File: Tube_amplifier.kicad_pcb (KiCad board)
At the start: 2 copper layers, 5 x 5 mm, 2 parts, among them U1 6N2P, U2 6P14P

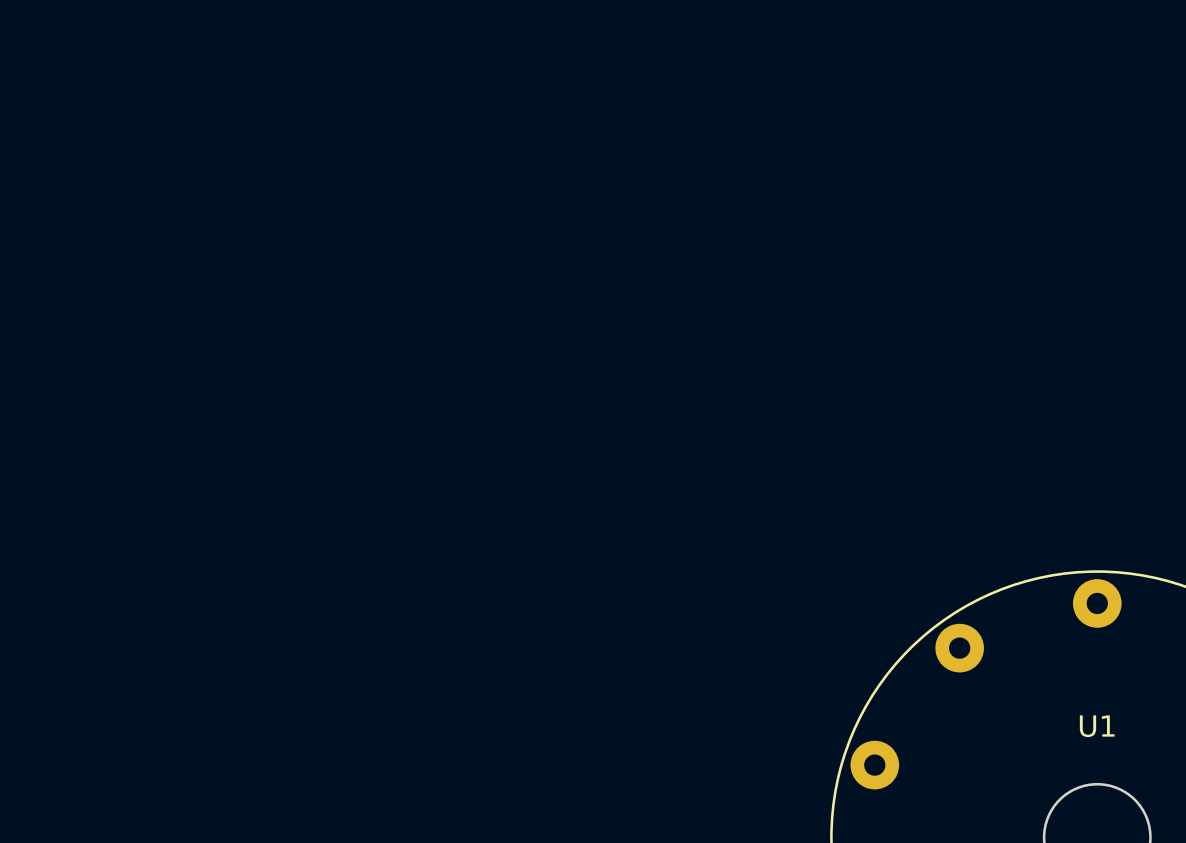
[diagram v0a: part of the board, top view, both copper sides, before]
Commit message: 7-pin socket 3d model added
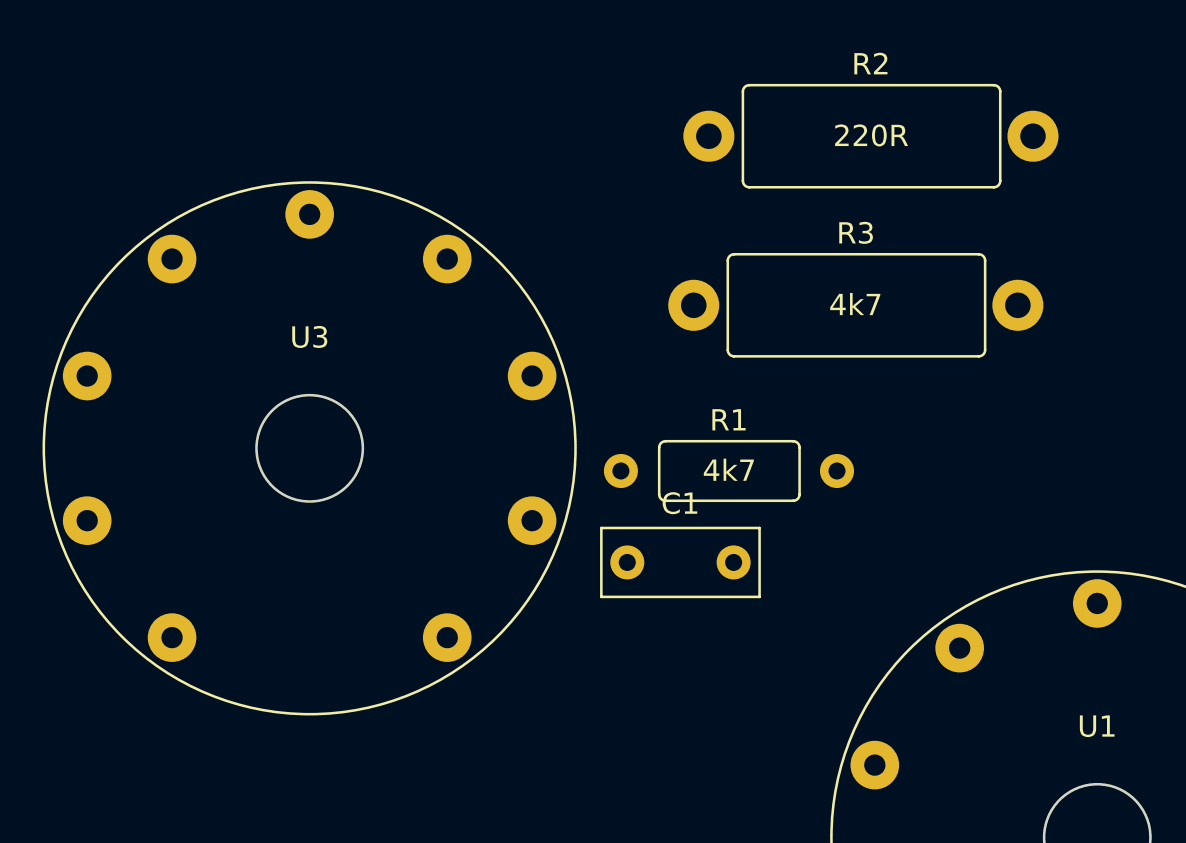
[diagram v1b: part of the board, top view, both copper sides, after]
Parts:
- added C1: 1500pF, Capacitor_THT:C_Rect_L7.2mm_W3.0mm_P5.00mm_FKS2_FKP2_MKS2_MKP2, F.Cu at (73.3, 48.1)
- added R1: 4k7, spdf1626_lib:R_THT_025W, F.Cu at (73.0, 43.8)
- added R2: 220R, spdf1626_lib:R_THT_1W, F.Cu at (77.1, 28.1)
- added R3: 4k7, spdf1626_lib:R_THT_1W, F.Cu at (76.4, 36.0)
- added U3: 6H2P, spdf1626_lib:9-pin_tube_socket, F.Cu at (58.4, 42.8)
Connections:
- U2 pad 3: unconnected-(U2-Pad3) -> Net-(U2-Pad3)
- U2 pad 7: unconnected-(U2-Pad7) -> Net-(U2-Pad7)

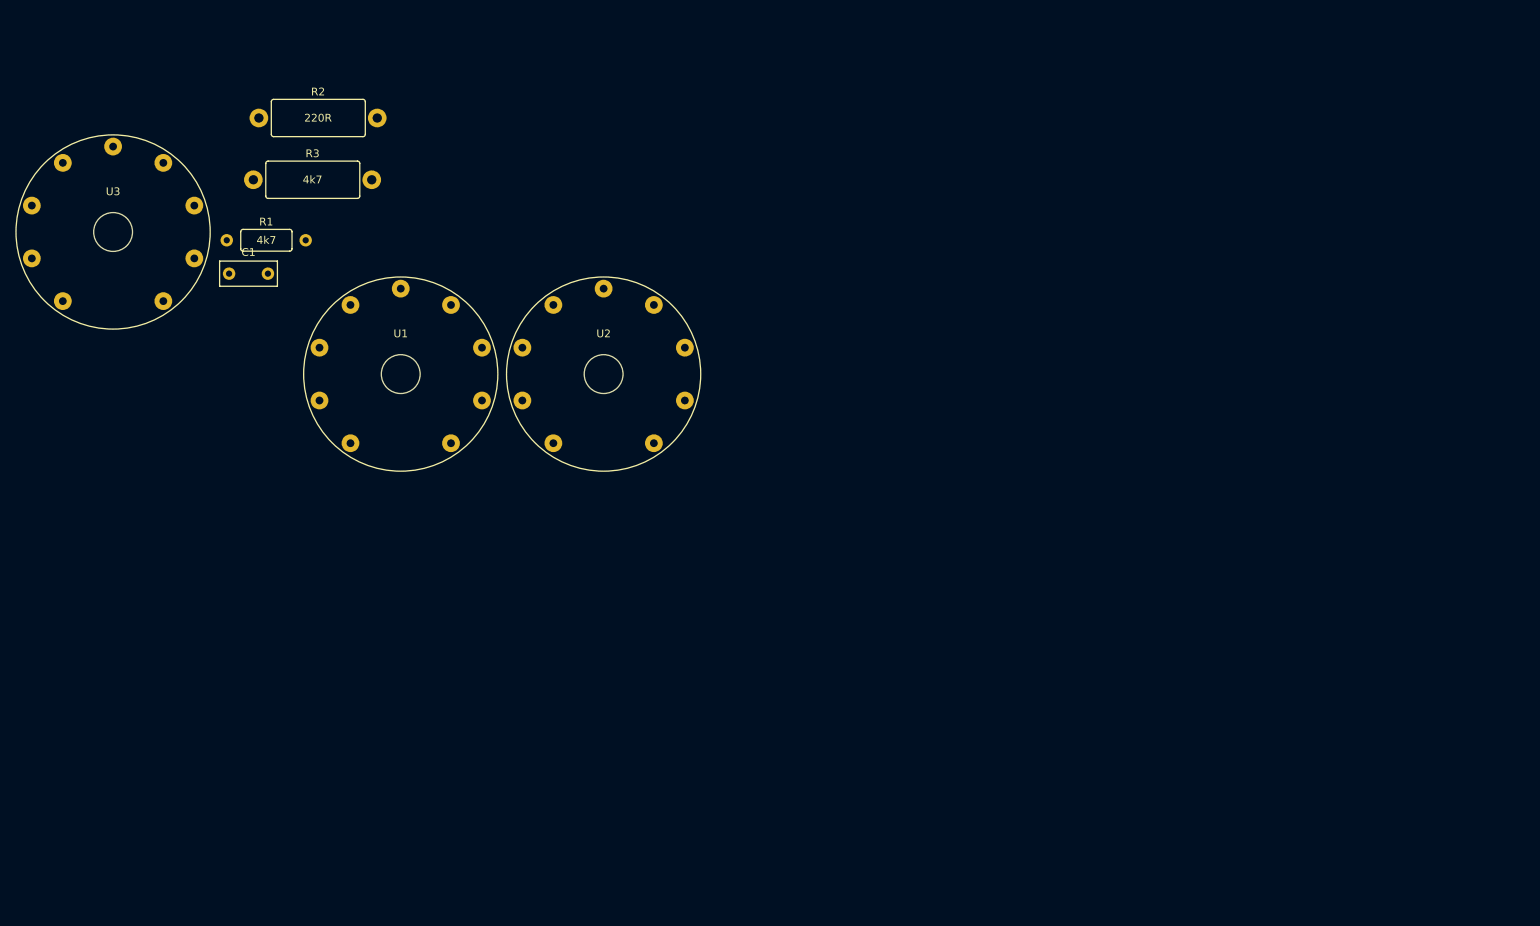
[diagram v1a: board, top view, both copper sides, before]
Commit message: Output transformer added, pcb v0.1 ready
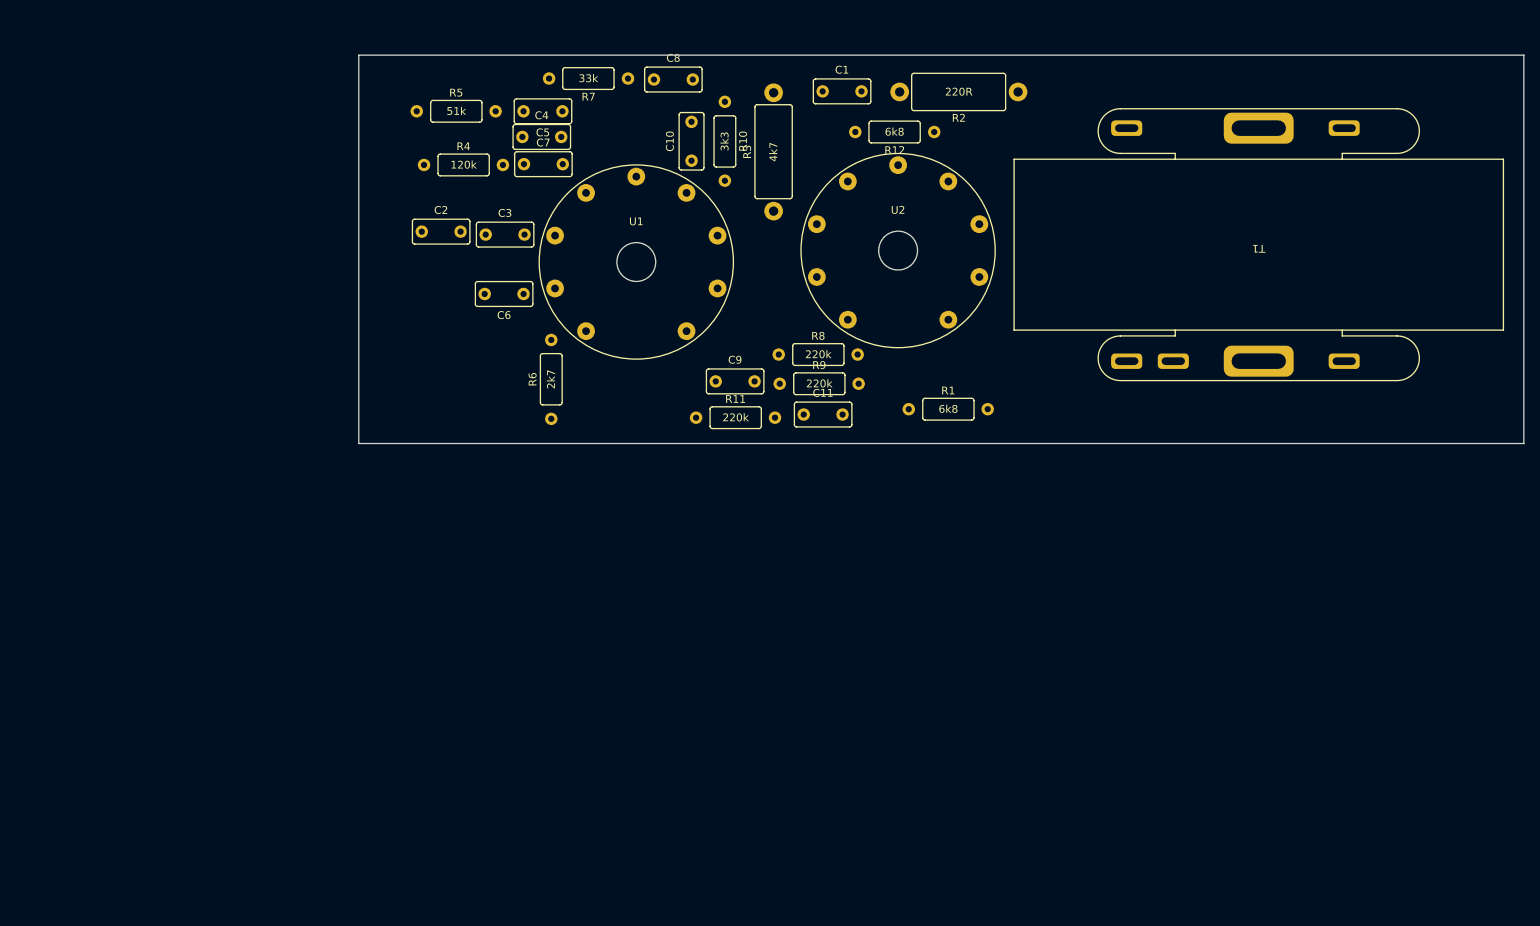
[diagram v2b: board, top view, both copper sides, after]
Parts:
- removed U3: 6H2P, spdf1626_lib:9-pin_tube_socket
- added C10: 2200pF, spdf1626_lib:C_THT_K73-17_P5.00mm, F.Cu at (132.8, 33.6)
- added C11: 3300pF, spdf1626_lib:C_THT_K73-17_P5.00mm, F.Cu at (147.3, 66.3)
- added C2: 0,047uF, spdf1626_lib:C_THT_K73-17_P5.00mm, F.Cu at (98.1, 42.7)
- added C3: 27pF, spdf1626_lib:C_THT_K73-17_P5.00mm, F.Cu at (106.3, 43.1)
- added C4: 2200pF, spdf1626_lib:C_THT_K73-17_P5.00mm, F.Cu at (111.1, 30.5)
- added C5: 4700pF, spdf1626_lib:C_THT_K73-17_P5.00mm, F.Cu at (116.2, 27.2)
- added C6: 0,01uF, spdf1626_lib:C_THT_K73-17_P5.00mm, F.Cu at (111.2, 50.7)
- added C7: 0,033uF, spdf1626_lib:C_THT_K73-17_P5.00mm, F.Cu at (111.3, 34.0)
- added C8: 2200pF, spdf1626_lib:C_THT_K73-17_P5.00mm, F.Cu at (128.0, 23.1)
- added C9: 5,6pF, spdf1626_lib:C_THT_K73-17_P5.00mm, F.Cu at (136.0, 62.0)
- added R10: 3k3, spdf1626_lib:R_THT_025W, F.Cu at (137.1, 26.0)
- added R11: 220k, spdf1626_lib:R_THT_025W, F.Cu at (133.4, 66.7)
- added R12: 6k8, spdf1626_lib:R_THT_025W, F.Cu at (164.1, 29.9)
- added R4: 120k, spdf1626_lib:R_THT_025W, F.Cu at (98.4, 34.1)
- added R5: 51k, spdf1626_lib:R_THT_025W, F.Cu at (97.5, 27.2)
- added R6: 2k7, spdf1626_lib:R_THT_025W, F.Cu at (114.8, 66.8)
- added R7: 33k, spdf1626_lib:R_THT_025W, F.Cu at (124.7, 23.0)
- added R8: 220k, spdf1626_lib:R_THT_025W, F.Cu at (144.1, 58.5)
- added R9: 220k, spdf1626_lib:R_THT_025W, F.Cu at (144.2, 62.3)
- added T1: Transformer_SP_1S, spdf1626_lib:Output_transformer, F.Cu at (205.9, 44.4)
- C1: footprint Capacitor_THT:C_Rect_L7.2mm_W3.0mm_P5.00mm_FKS2_FKP2_MKS2_MKP2 -> spdf1626_lib:C_THT_K73-17_P5.00mm
- R1: value 4k7 -> 6k8
- moved R2 97.8 mm to (174.9, 24.7), turned to 180 degrees
- moved R1 90.5 mm to (160.8, 65.6)
- moved C1 79.9 mm to (149.7, 24.7)
- moved R3 67.1 mm to (143.4, 40.1), turned to 90 degrees
- moved U2 41.1 mm to (159.4, 45.2)
- moved U1 33.6 mm to (125.7, 46.6)
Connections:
- R1 pad 1: unconnected-(R1-Pad1) -> Net-(R1-Pad1)
- R1 pad 2: unconnected-(R1-Pad2) -> Net-(R1-Pad2)
- U1 pad 1: unconnected-(U1-Pad1) -> Net-(U1-Pad1)
- U1 pad 2: unconnected-(U1-Pad2) -> Net-(U1-Pad2)
- U1 pad 3: unconnected-(U1-Pad3) -> Net-(U1-Pad3)
- U1 pad 4: unconnected-(U1-Pad4) -> +6V
- U1 pad 5: unconnected-(U1-Pad5) -> GND
- U1 pad 6: unconnected-(U1-Pad6) -> Net-(U1-Pad6)
- U1 pad 7: unconnected-(U1-Pad7) -> Net-(U1-Pad7)
- U1 pad 8: unconnected-(U1-Pad8) -> Net-(U1-Pad8)
- U2 pad 2: unconnected-(U2-Pad2) -> Net-(R1-Pad2)
- U2 pad 4: unconnected-(U2-Pad4) -> +6V
- U2 pad 5: unconnected-(U2-Pad5) -> GND
- U2 pad 9: unconnected-(U2-Pad9) -> Net-(U2-Pad9)
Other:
- board size 5 x 5 mm -> 150 x 50 mm

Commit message: 7-pin tube socket added
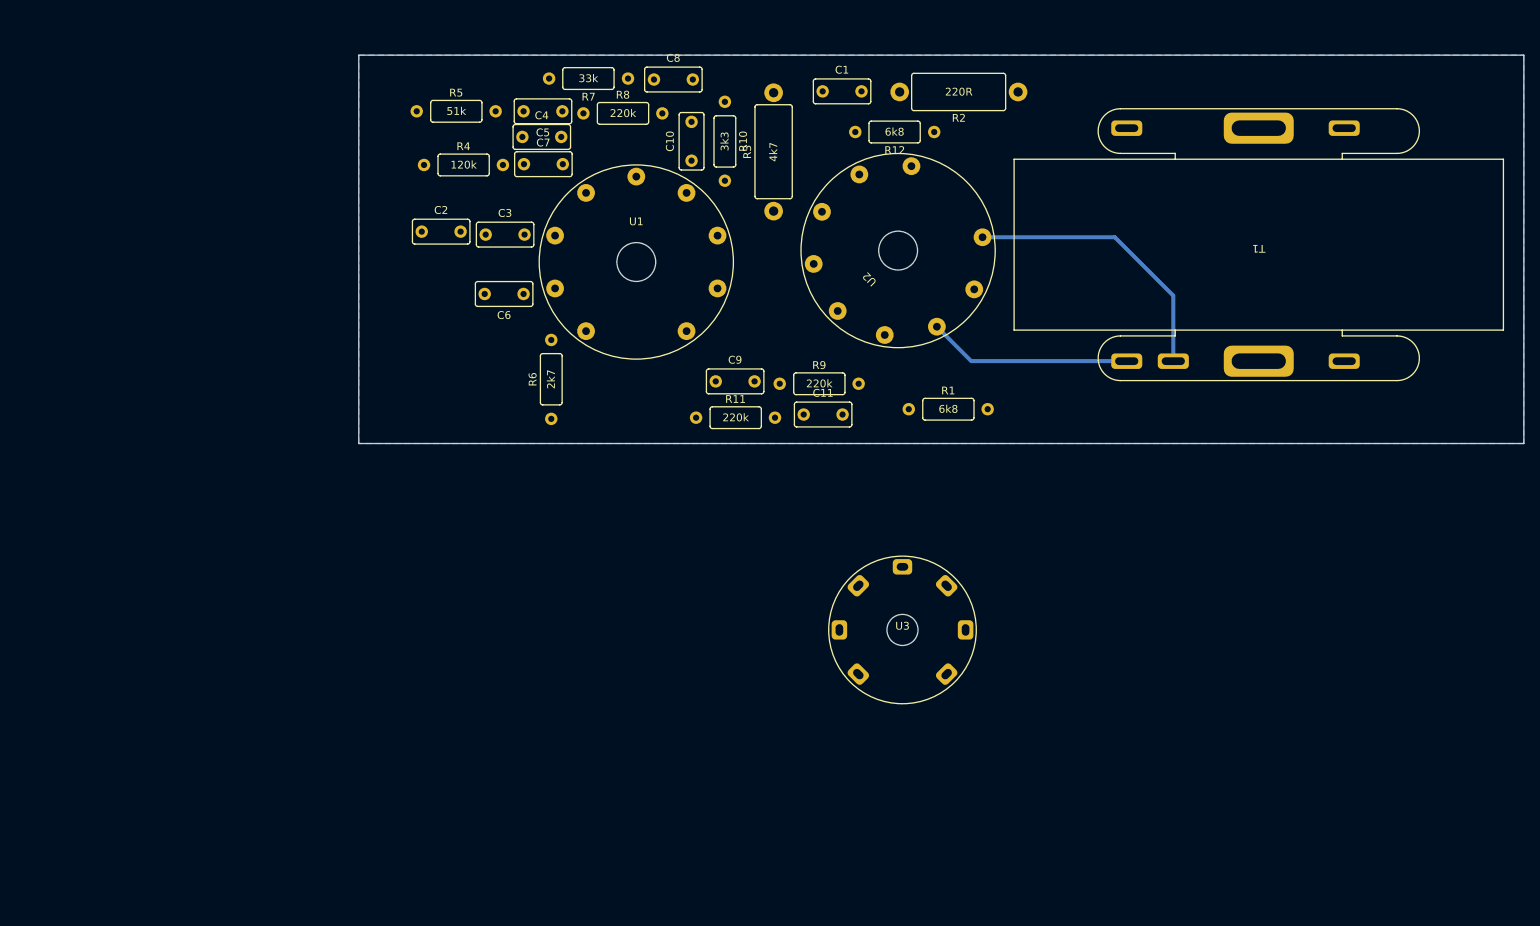
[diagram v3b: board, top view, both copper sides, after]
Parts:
- added U3: 6H2P, spdf1626_lib:7-pin_tube_socket, F.Cu at (160.0, 94.0)
- moved R8 40.0 mm to (118.9, 27.5)
- turned U2 to 135 degrees
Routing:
- net Net-(T1-Pad2): track 0.00 -> 36.1 mm
- net Net-(R3-Pad1): track 0.00 -> 26.3 mm
- added copper zone on B.Cu, net GND

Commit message: Amplifier ready
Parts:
- removed U3: 6H2P, spdf1626_lib:7-pin_tube_socket
- added C12: 10uF, spdf1626_lib:C_THT_D10.0mm_P5.00mm, F.Cu at (177.0, 65.8)
- added C13: 10uF, spdf1626_lib:C_THT_D10.0mm_P5.00mm, F.Cu at (140.0, 63.0)
- added J2: Input, spdf1626_lib:PinHeader_1x02_P2.54mm, F.Cu at (93.5, 55.5)
- added J3: Conn_01x04, spdf1626_lib:PinHeader_1x04_P2.54mm, F.Cu at (158.7, 65.0)
- added J4: output, spdf1626_lib:PinHeader_1x02_P2.54mm, F.Cu at (232.0, 24.0)
- added RV1: 470k, spdf1626_lib:PinHeader_1x03_P2.54mm, F.Cu at (93.5, 65.5)
- added RV2: 2,2M, spdf1626_lib:Potentiometer_THT_CA9V, F.Cu at (97.7, 37.8)
- added RV3: 1M, spdf1626_lib:Potentiometer_THT_CA9V, F.Cu at (136.5, 25.0)
- moved R11 44.8 mm to (158.4, 29.5)
- moved R1 42.2 mm to (149.5, 24.9), turned to -90 degrees
- moved C1 39.4 mm to (151.0, 64.0), turned to 90 degrees
- moved C9 38.3 mm to (146.0, 25.0), turned to -90 degrees
- moved C11 36.7 mm to (153.0, 30.0), turned to 90 degrees
- moved R2 34.0 mm to (144.5, 40.0), turned to -90 degrees
- moved R3 33.8 mm to (170.0, 61.0), turned to 180 degrees
- moved R8 32.9 mm to (134.5, 56.5), turned to -90 degrees
- moved R10 25.9 mm to (111.4, 29.0), turned to 0 degrees
- moved C6 20.5 mm to (126.0, 65.0)
- moved R9 19.8 mm to (140.0, 43.0), turned to -90 degrees
- moved R12 16.6 mm to (179.6, 24.0)
- moved C10 16.4 mm to (116.5, 32.5), turned to 180 degrees
- moved C7 15.4 mm to (103.0, 47.0)
- moved C3 15.1 mm to (104.0, 58.0), turned to -90 degrees
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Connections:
- C2 pad 1: Left_input -> Net-(C2-Pad1)
- R11 pad 1: GND -> Net-(C11-Pad2)
- R11 pad 2: Net-(C11-Pad2) -> GND
- T1 pad 4: GND -> Left_output
- T1 pad 5: Left_output -> GND
- U1 pad 9: unconnected-(U1-Pad9) -> GND
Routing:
- net 240V: track 0.00 -> 104.7 mm
- net Net-(C10-Pad1): track 0.00 -> 70.3 mm
- net +6V: track 0.00 -> 65.7 mm
- net Left_output: track 0.00 -> 59.4 mm
- net Net-(C3-Pad2): track 0.00 -> 31.2 mm
- net Net-(C7-Pad2): track 0.00 -> 30.4 mm
- net Net-(C11-Pad1): track 0.00 -> 28.6 mm
- net Net-(C4-Pad2): track 0.00 -> 24.3 mm
- net Net-(C8-Pad1): track 0.00 -> 18.2 mm
- net Net-(C4-Pad1): track 0.00 -> 14.4 mm
- net Net-(C2-Pad2): track 0.00 -> 11.5 mm
- net Net-(RV3-Pad2): track 0.00 -> 11.2 mm
- net Net-(C5-Pad2): track 0.00 -> 11.0 mm
- net Net-(C11-Pad2): track 0.00 -> 10.8 mm
- net Net-(C6-Pad1): track 0.00 -> 10.7 mm
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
